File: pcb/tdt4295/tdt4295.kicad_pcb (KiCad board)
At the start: 6 copper layers, 209.6 x 139.7 mm, 170 parts, among them J101 ARM 20 Pin Debug Header, J102 MCU USART1 Header, J103 DM1AA-SF-PEJ(21), J104 MCU GPIO Header, J301 FPGA__debug, J501 618015330923, J502 FPGA GPIO, P201 690-005-299-043, U101 EFM32GG12B810F1024GQ64, U102 COM-09032 Joystick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

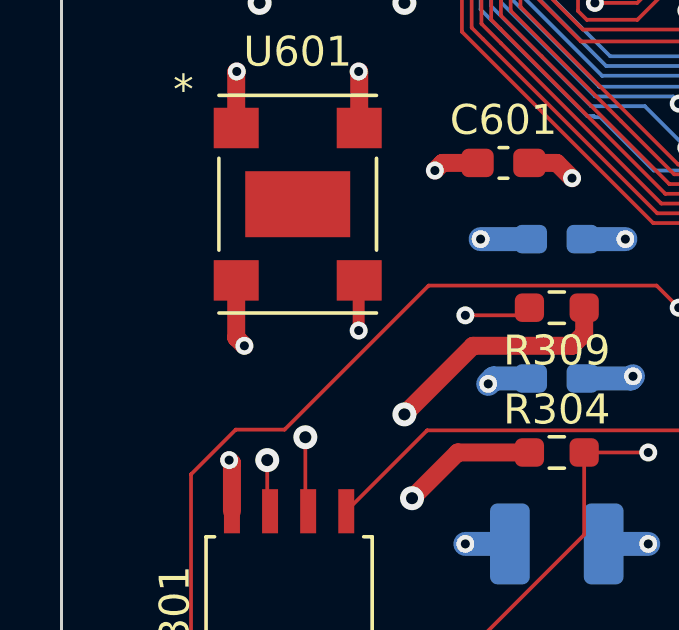
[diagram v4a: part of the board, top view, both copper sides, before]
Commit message: fix the remainder of DRC problems
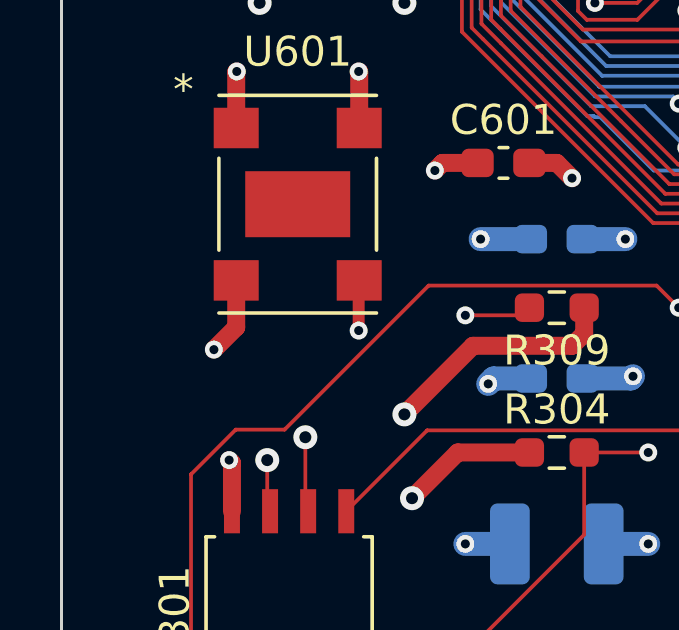
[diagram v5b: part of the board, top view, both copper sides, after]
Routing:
- net +3V3: track 848.7 -> 880.1 mm
- net GND: track 471.5 -> 477.3 mm
- net +1V8: track 211.6 -> 211.1 mm
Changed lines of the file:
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@@
     (thickness 1.6)
     (drawings 19)
-    (tracks 2879)
+    (tracks 2880)
     (zones 0)
     (modules 170)
@@
   (layers
     (0 F.Cu signal)
-    (1 +PWR power hide)
+    (1 +PWR power)
     (2 GND power hide)
     (3 In3.Cu signal)
@@
   )
   (setup
-    (last_trace_width 0.125)
+    (last_trace_width 0.3)
     (user_trace_width 0.125)
     (user_trace_width 0.2)
@@
     (effects (font (size 1.5 1.5) (thickness 0.3)) (justify left))
   )
-  (segment (start 64.135 35.56) (end 83.82 35.56) (width 0.8) (layer +PWR) (net 2))
   (segment (start 85.1582 71.289304) (end 84.656815 71.790689) (width 0.3) (layer F.Cu) (net 1))
   (segment (start 85.1582 71.16508) (end 85.1582 71.289304) (width 0.3) (layer F.Cu) (net 1))
@@
   (segment (start 66.5745 82.677) (end 65.405 82.677) (width 0.6) (layer F.Cu) (net 1))
   (via (at 65.151 82.931) (size 0.6) (drill 0.3) (layers F.Cu B.Cu) (net 1))
-  (segment (start 58.529002 88.501002) (end 58.801 88.773) (width 0.6) (layer F.Cu) (net 1))
-  (segment (start 58.529002 86.59288) (end 58.529002 88.501002) (width 0.6) (layer F.Cu) (net 1))
-  (via (at 58.801 88.773) (size 0.6) (drill 0.3) (layers F.Cu B.Cu) (net 1))
   (segment (start 82.1582 80.16508) (end 82.19708 80.16508) (width 0.3) (layer F.Cu) (net 1))
   (via (at 82.495376 80.491752) (size 0.6) (drill 0.3) (layers F.Cu B.Cu) (net 1))
@@
   (via (at 127.367504 81.647504) (size 0.8) (drill 0.4) (layers F.Cu B.Cu) (net 1))
   (segment (start 125.019999 88.225) (end 125.019999 83.995009) (width 0.3) (layer F.Cu) (net 1))
+  (segment (start 76.864174 80.615826) (end 75.565 81.915) (width 0.6) (layer GND) (net 1))
+  (segment (start 80.592161 80.615826) (end 76.864174 80.615826) (width 0.6) (layer GND) (net 1))
+  (via (at 57.785 88.9) (size 0.6) (drill 0.3) (layers F.Cu B.Cu) (net 1))
+  (segment (start 58.529002 86.59288) (end 58.529002 88.155998) (width 0.6) (layer F.Cu) (net 1))
+  (segment (start 58.529002 88.155998) (end 57.785 88.9) (width 0.6) (layer F.Cu) (net 1))
+  (segment (start 64.135 35.56) (end 83.82 35.56) (width 0.8) (layer +PWR) (net 2))
   (via (at 90.589792 75.573631) (size 0.6) (drill 0.3) (layers F.Cu B.Cu) (net 2))
   (segment (start 90.181241 75.16508) (end 90.589792 75.573631) (width 0.3) (layer F.Cu) (net 2))
@@
   (segment (start 195.898998 43.561) (end 189.167998 36.83) (width 0.6) (layer +PWR) (net 2))
   (segment (start 228.473 43.561) (end 195.898998 43.561) (width 0.6) (layer +PWR) (net 2))
-  (segment (start 145.415 113.03) (end 127.707719 130.737281) (width 0.6) (layer +PWR) (net 2))
+  (segment (start 145.415 113.03) (end 127.707719 130.737281) (width 0.8) (layer +PWR) (net 2))
   (segment (start 82.423 143.437281) (end 95.123 130.737281) (width 0.6) (layer +PWR) (net 2))
   (segment (start 95.123 130.737281) (end 95.177281 130.737281) (width 0.6) (layer +PWR) (net 2))
-  (segment (start 95.177281 130.737281) (end 74.803 130.737281) (width 0.6) (layer +PWR) (net 2))
-  (segment (start 127.707719 130.737281) (end 95.177281 130.737281) (width 0.6) (layer +PWR) (net 2))
+  (segment (start 95.177281 130.737281) (end 74.803 130.737281) (width 0.8) (layer +PWR) (net 2))
+  (segment (start 127.707719 130.737281) (end 95.177281 130.737281) (width 0.8) (layer +PWR) (net 2))
   (segment (start 257.81 113.03) (end 225.298 113.03) (width 0.6) (layer F.Cu) (net 2))
   (via (at 257.81 113.03) (size 0.8) (drill 0.4) (layers F.Cu B.Cu) (net 2))
@@
   (segment (start 59.309 77.343) (end 60.325 77.343) (width 0.6) (layer +PWR) (net 2))
   (segment (start 64.135 79.375) (end 64.135 77.343022) (width 0.6) (layer +PWR) (net 2))
-  (segment (start 58.293 90.465002) (end 64.135 84.623002) (width 0.6) (layer +PWR) (net 2))
+  (segment (start 58.293 90.465002) (end 64.135 84.623002) (width 0.8) (layer +PWR) (net 2))
   (segment (start 58.293 92.583) (end 58.293 90.465002) (width 0.6) (layer +PWR) (net 2))
   (segment (start 64.135 84.623002) (end 64.135 84.455) (width 0.6) (layer +PWR) (net 2))
   (segment (start 64.135 91.059) (end 64.135 84.455) (width 0.6) (layer +PWR) (net 2))
-  (segment (start 57.492999 91.265003) (end 58.293 90.465002) (width 0.6) (layer +PWR) (net 2))
-  (segment (start 57.492999 106.768999) (end 57.492999 91.265003) (width 0.6) (layer +PWR) (net 2))
-  (segment (start 58.039 107.315) (end 57.492999 106.768999) (width 0.6) (layer +PWR) (net 2))
-  (segment (start 69.723 83.185012) (end 69.723 82.042) (width 0.6) (layer +PWR) (net 2))
-  (segment (start 69.723 82.042) (end 72.39 79.375) (width 0.6) (layer +PWR) (net 2))
+  (segment (start 69.723 83.185012) (end 69.723 82.042) (width 0.8) (layer +PWR) (net 2))
+  (segment (start 69.723 82.042) (end 72.39 79.375) (width 0.8) (layer +PWR) (net 2))
   (segment (start 69.723 82.042) (end 69.723 81.788) (width 0.6) (layer +PWR) (net 2))
-  (segment (start 65.289001 69.559001) (end 64.459 68.729) (width 0.6) (layer +PWR) (net 2))
-  (segment (start 65.289001 77.354001) (end 65.289001 69.559001) (width 0.6) (layer +PWR) (net 2))
-  (segment (start 69.723 81.788) (end 65.289001 77.354001) (width 0.6) (layer +PWR) (net 2))
-  (segment (start 65.289001 78.220999) (end 64.135 79.375) (width 0.6) (layer +PWR) (net 2))
-  (segment (start 65.289001 77.354001) (end 65.289001 78.220999) (width 0.6) (layer +PWR) (net 2))
   (segment (start 64.135 81.153) (end 64.135 81.28) (width 0.6) (layer +PWR) (net 2))
   (segment (start 62.611 79.629) (end 64.135 81.153) (width 0.6) (layer +PWR) (net 2))
-  (segment (start 64.135 81.28) (end 64.135 79.375) (width 0.6) (layer +PWR) (net 2))
-  (segment (start 64.135 84.455) (end 64.135 81.28) (width 0.6) (layer +PWR) (net 2))
+  (segment (start 64.135 81.28) (end 64.135 79.375) (width 0.8) (layer +PWR) (net 2))
+  (segment (start 64.135 84.455) (end 64.135 81.28) (width 0.8) (layer +PWR) (net 2))
   (segment (start 125.667089 73.723654) (end 126.635011 74.691576) (width 0.8) (layer +PWR) (net 2))
   (segment (start 126.635011 74.691576) (end 126.635011 80.899997) (width 0.8) (layer +PWR) (net 2))
@@
   (segment (start 135.255 92.075) (end 131.445 92.075) (width 0.8) (layer +PWR) (net 2))
   (segment (start 105.537 73.279) (end 105.537 81.915) (width 0.6) (layer +PWR) (net 2))
-  (segment (start 61.595 65.865) (end 61.595 44.45) (width 0.6) (layer +PWR) (net 2))
-  (segment (start 64.459 68.729) (end 61.595 65.865) (width 0.6) (layer +PWR) (net 2))
+  (segment (start 61.595 65.865) (end 61.595 44.45) (width 0.8) (layer +PWR) (net 2))
+  (segment (start 64.459 68.729) (end 61.595 65.865) (width 0.8) (layer +PWR) (net 2))
+  (segment (start 74.803 124.079) (end 58.039 107.315) (width 0.8) (layer +PWR) (net 2))
+  (segment (start 74.803 130.737281) (end 74.803 124.079) (width 0.8) (layer +PWR) (net 2))
+  (segment (start 56.515 92.243002) (end 58.293 90.465002) (width 0.8) (layer +PWR) (net 2))
+  (segment (start 56.515 105.791) (end 56.515 92.243002) (width 0.8) (layer +PWR) (net 2))
+  (segment (start 58.039 107.315) (end 56.515 105.791) (width 0.8) (layer +PWR) (net 2))
+  (segment (start 66.04 77.47) (end 64.135 79.375) (width 0.8) (layer +PWR) (net 2))
+  (segment (start 66.04 70.31) (end 64.459 68.729) (width 0.8) (layer +PWR) (net 2))
+  (segment (start 66.04 78.105) (end 66.04 70.31) (width 0.8) (layer +PWR) (net 2))
+  (segment (start 69.723 81.788) (end 66.04 78.105) (width 0.8) (layer +PWR) (net 2))
   (segment (start 135.255 78.275) (end 135.255 80.010002) (width 0.3) (layer B.Cu) (net 3))
   (via (at 135.255 80.010002) (size 0.8) (drill 0.4) (layers F.Cu B.Cu) (net 3))
@@
   (segment (start 86.487 83.613798) (end 84.240601 81.367399) (width 0.8) (layer +PWR) (net 7))
   (segment (start 83.454999 86.979001) (end 86.487 83.947) (width 0.8) (layer +PWR) (net 7))
-  (segment (start 77.089 92.075) (end 76.581 92.075) (width 0.8) (layer +PWR) (net 7))
   (segment (start 96.947003 100.949001) (end 79.105001 100.949001) (width 0.8) (layer +PWR) (net 7))
   (segment (start 142.875 98.425) (end 141.239999 100.060001) (width 0.8) (layer +PWR) (net 7))
@@
   (segment (start 120.055 81.3) (end 118.852 81.3) (width 0.125) (layer F.Cu) (net 127))
   (via (at 93.836252 76.597748) (size 0.6) (drill 0.3) (layers F.Cu B.Cu) (net 127))
-  (segment (start 93.345 76.106496) (end 93.836252 76.597748) (width 0.125) (layer In3.Cu) (net 127))
-  (segment (start 93.345 76.073) (end 93.345 76.106496) (width 0.125) (layer In3.Cu) (net 127))
-  (segment (start 93.2434 75.9714) (end 93.345 76.073) (width 0.125) (layer In3.Cu) (net 127))
-  (segment (start 91.977427 75.9714) (end 93.2434 75.9714) (width 0.125) (layer In3.Cu) (net 127))
-  (segment (start 89.627059 73.621032) (end 91.977427 75.9714) (width 0.125) (layer In3.Cu) (net 127))
   (segment (start 97.982052 78.170052) (end 99.187 79.375) (width 0.125) (layer B.Cu) (net 127))
   (via (at 108.839 80.391) (size 0.6) (drill 0.3) (layers F.Cu B.Cu) (net 127))
@@
   (segment (start 109.748 81.3) (end 120.095 81.3) (width 0.125) (layer F.Cu) (net 127))
   (segment (start 108.839 80.391) (end 109.748 81.3) (width 0.125) (layer F.Cu) (net 127))
+  (segment (start 93.345 76.106496) (end 93.836252 76.597748) (width 0.125) (layer In3.Cu) (net 127))
+  (segment (start 93.209904 75.9714) (end 93.345 76.106496) (width 0.125) (layer In3.Cu) (net 127))
+  (segment (start 91.977427 75.9714) (end 93.209904 75.9714) (width 0.125) (layer In3.Cu) (net 127))
+  (segment (start 89.627059 73.621032) (end 91.977427 75.9714) (width 0.125) (layer In3.Cu) (net 127))
   (segment (start 92.358199 77.365079) (end 92.1582 77.16508) (width 0.125) (layer F.Cu) (net 128))
   (segment (start 93.830921 77.365079) (end 92.358199 77.365079) (width 0.125) (layer F.Cu) (net 128))

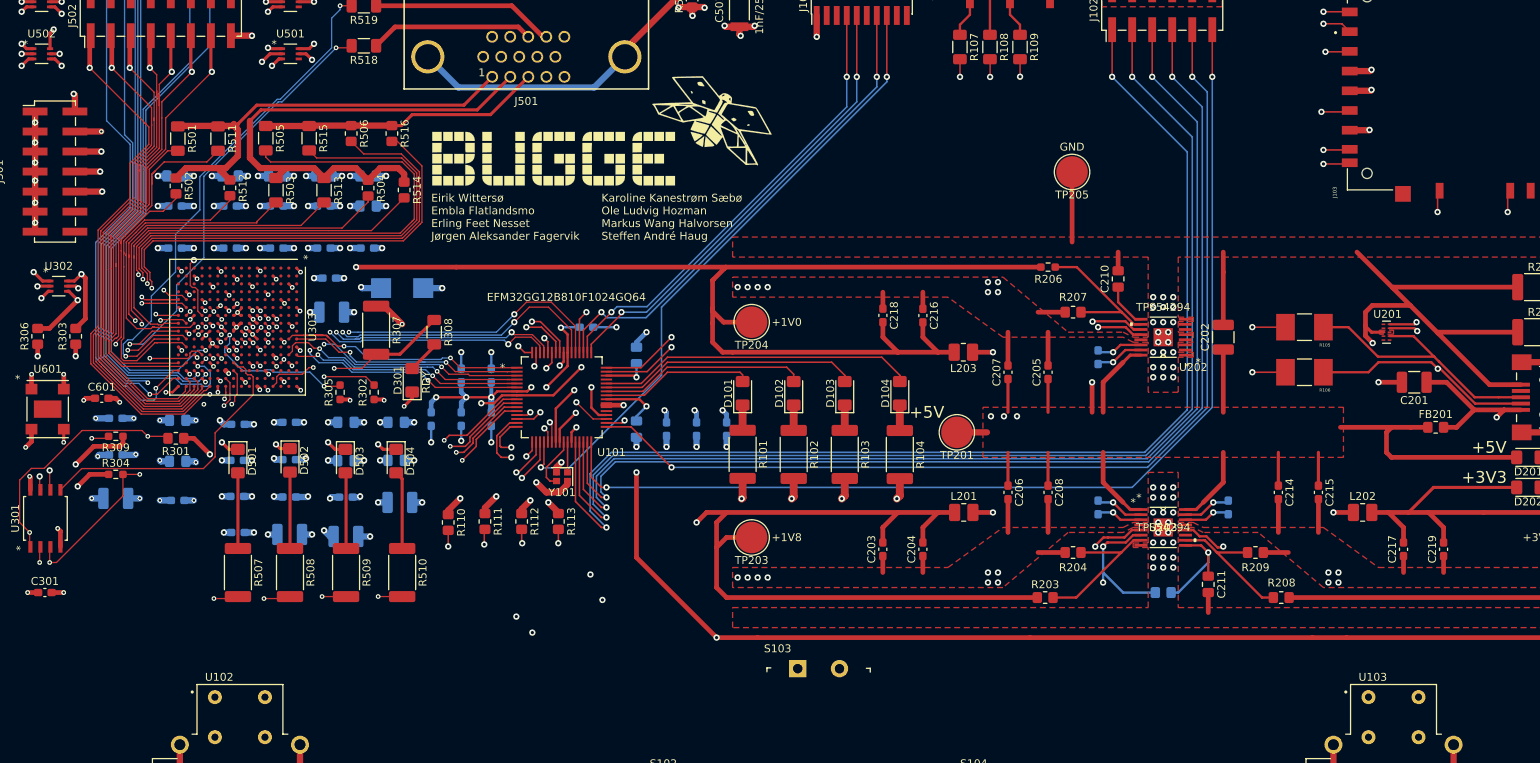
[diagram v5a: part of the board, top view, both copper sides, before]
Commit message: more routing cleanup
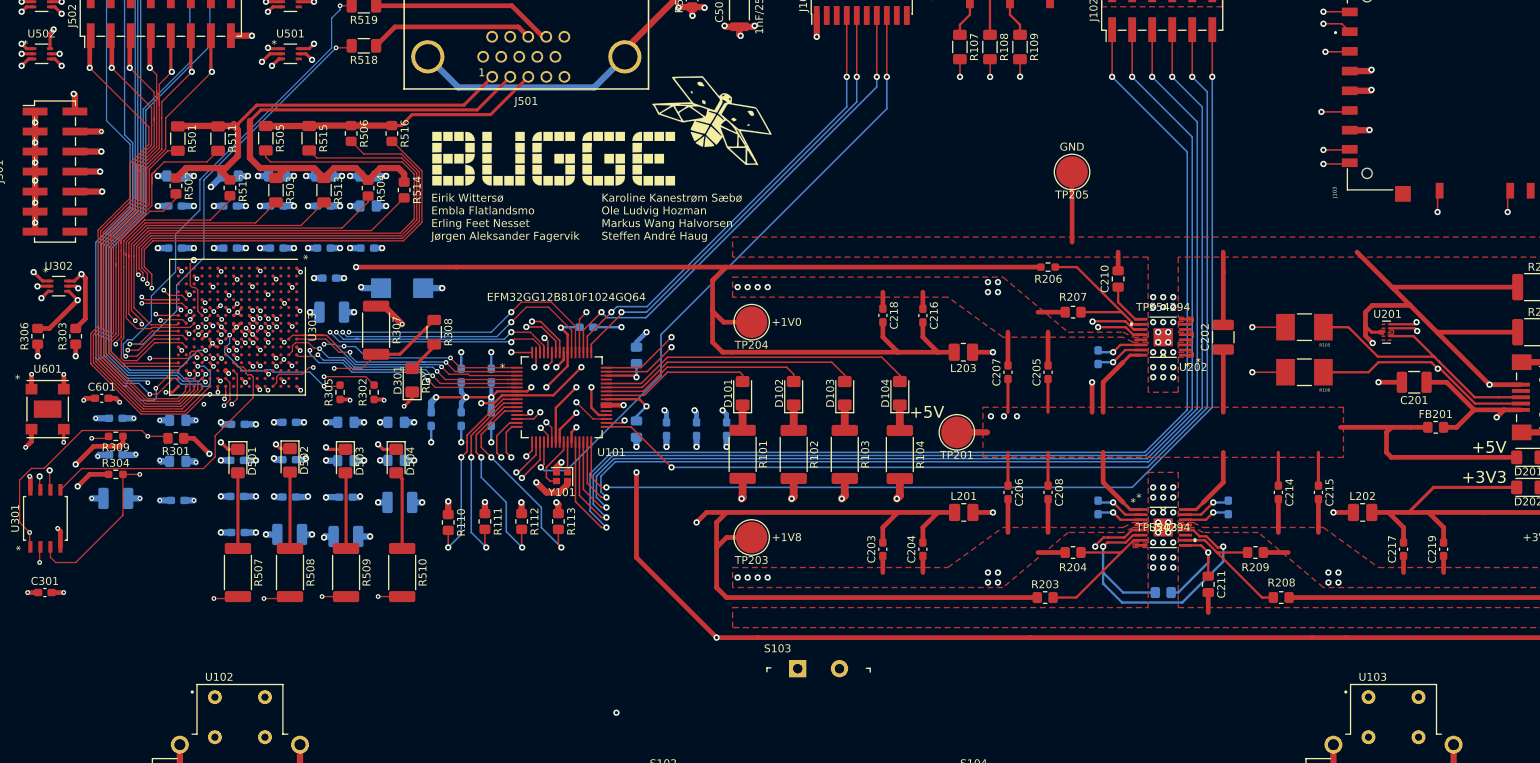
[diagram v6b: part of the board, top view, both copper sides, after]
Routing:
- net +3V3: track 880.1 -> 902.3 mm
- net +1V0: track 181.9 -> 193.9 mm
- net FPGA_PROGRAM_B: track 60.5 -> 70.8 mm
- net FPGA_DONE: track 66.0 -> 72.4 mm
- net GPIO_PB12: track 88.2 -> 82.1 mm
- net GPIO_PB11: track 93.8 -> 87.7 mm
- net SDIO_WP: track 144.4 -> 139.4 mm
- net GND: track 477.3 -> 481.0 mm, vias 204 -> 205
- net GPIO_BTN3: track 92.0 -> 88.8 mm, vias 4 -> 2
- net GPIO_BTN1: track 65.9 -> 63.0 mm
- net GPIO_BTN0: track 91.5 -> 94.2 mm, vias 4 -> 3
- net GPIO_BTN2: track 69.5 -> 66.9 mm
- net +1V8: track 211.1 -> 213.3 mm
- net SDIO_CMD: track 123.1 -> 124.8 mm
- net /FPGA/IOB14/QSPI_DQ2: track 38.0 -> 38.9 mm, vias 3 -> 2
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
